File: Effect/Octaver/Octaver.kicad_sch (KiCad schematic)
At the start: 25 parts, among them J1 Conn_01x04_Pin, J2 Conn_01x04_Pin, Q1 MMBF5103, Q2 DMMT5551

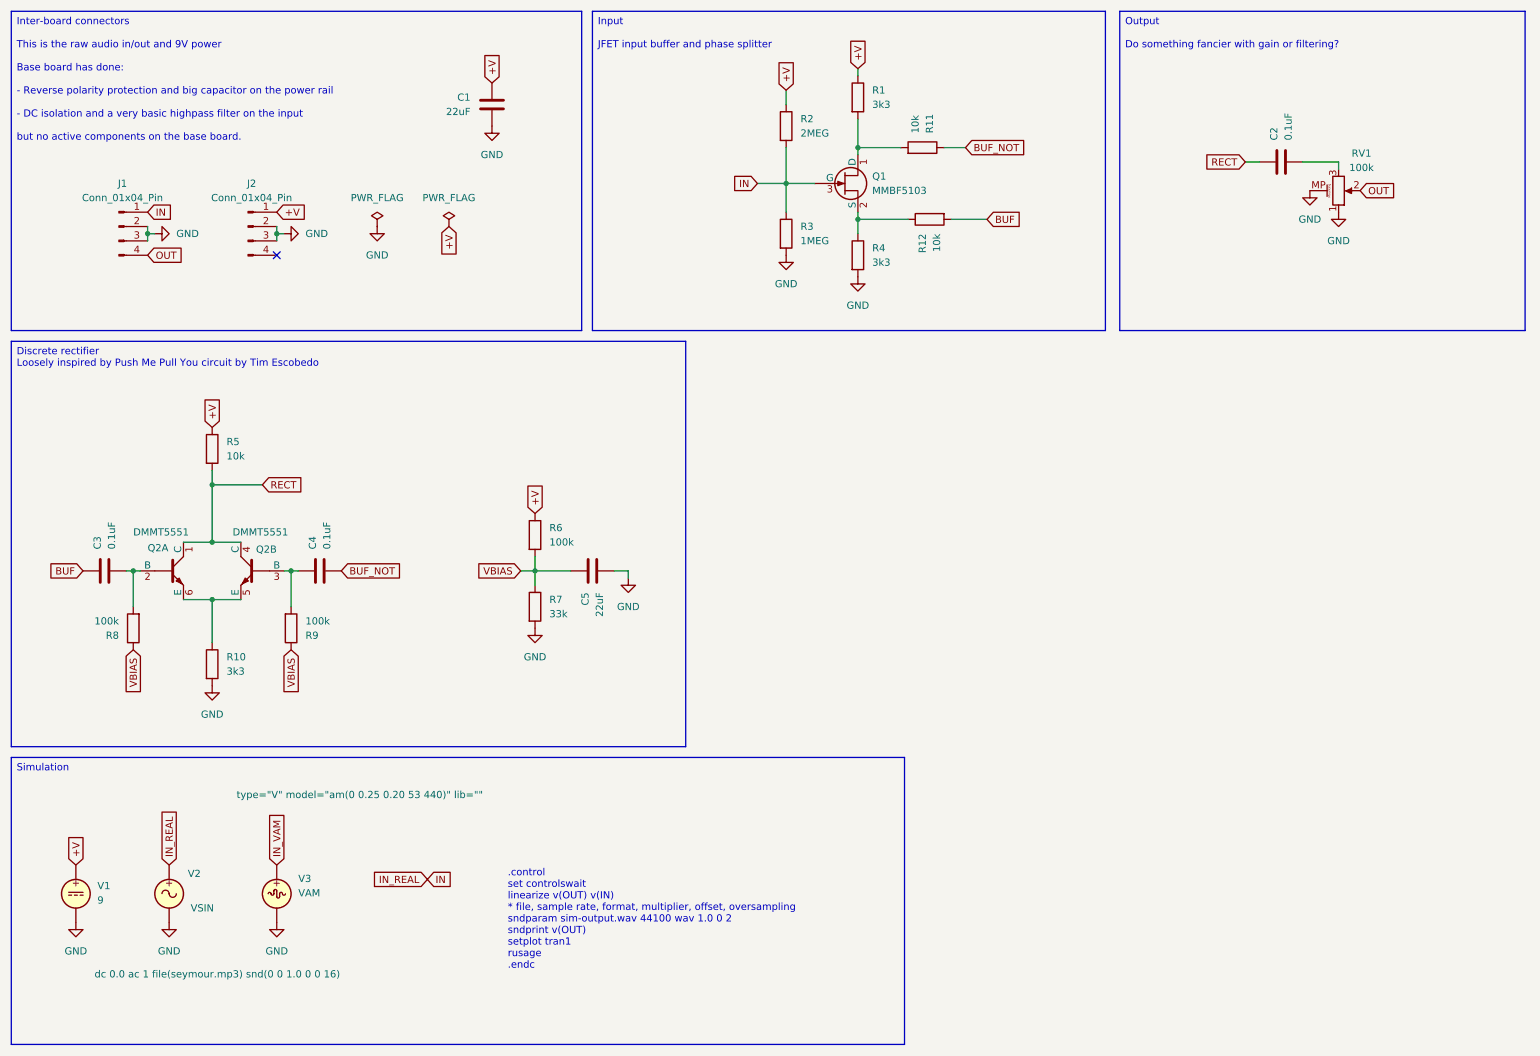
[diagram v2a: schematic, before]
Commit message: Update the Octaver circuit more, improve simulation
When I was trying to look up JFET phase splitter cicuits, I came up
suspiciously empty.  Adding the resistors between the phase splitter and
the rectification stage did fix things in simulation, but it all makes
me think somebody knows more than I do about this.

So since I wanted some amplification anyway, I put another BJT stage
there for the phase splitting, and one in the output stage for
amplification.

And I added the base board to the simulation, so that the whole input
signal rebiasing actually shows up for real.  With the DC-blocking
capacitor no longer on the effects board, the simulation ended up seeing
the signal input as a power source and that then made things all wonky.

Now, this is why I don't use op-amps any more: sane people do op-amp
circuits so that they don't have to worry about impedance issues.  But
insane people like me want to learn about these things, so...

That said, I think I really need to learn about feedback.  And not just
the "emitter degeneration resistor" kind.  Actual feedback between
stages (or even just from output back to transistor gate voltage for a
single transistor stage).

Signed-off-by: Linus Torvalds <torvalds@linux-foundation.org>
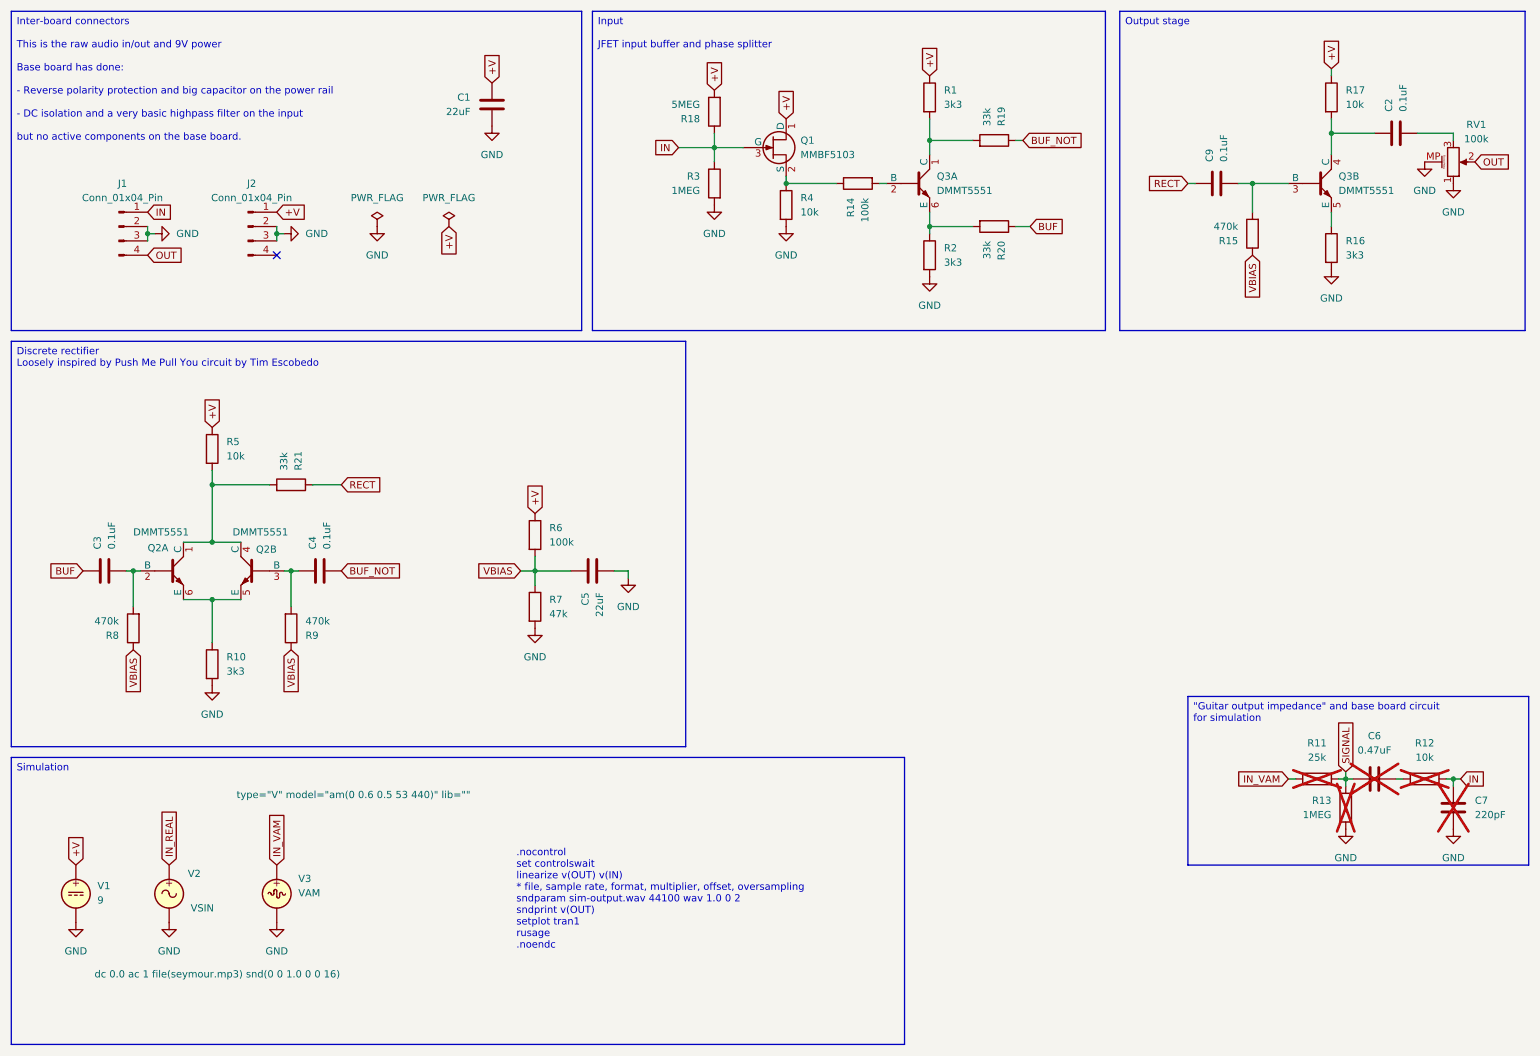
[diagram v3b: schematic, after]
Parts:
- added C6: 0.47uF, Capacitor_SMD:C_1206_3216Metric, symbol Device:C
- added C7: 220pF, Capacitor_SMD:C_0805_2012Metric_Pad1.18x1.45mm_HandSolder, symbol Device:C
- added C9: 0.1uF, Mylib:C_0704_1810Metric, symbol Device:C
- added Q3: DMMT5551, Package_TO_SOT_SMD:SOT-23-6, symbol Mylib:DMMT5551
- added R13: 1MEG, Resistor_SMD:R_0805_2012Metric, symbol Device:R
- added R14: 100k, Resistor_SMD:R_0805_2012Metric, symbol Device:R
- added R15: 470k, Resistor_SMD:R_0805_2012Metric, symbol Device:R
- added R16: 3k3, Resistor_SMD:R_0805_2012Metric, symbol Device:R
- added R17: 10k, Resistor_SMD:R_0805_2012Metric, symbol Device:R
- added R18: 5MEG, Resistor_SMD:R_0805_2012Metric, symbol Device:R
- added R19, R20, R21: 33k, Resistor_SMD:R_0805_2012Metric, symbol Device:R
- R11: value 10k -> 25k; footprint Resistor_SMD:R_0805_2012Metric -> Resistor_SMD:R_0805_2012Metric_Pad1.20x1.40mm_HandSolder; now not fitted; now left out of the parts list
- R12: footprint Resistor_SMD:R_0805_2012Metric -> Resistor_SMD:R_0805_2012Metric_Pad1.20x1.40mm_HandSolder; now not fitted; now left out of the parts list
- R2: value 2MEG -> 3k3
- R4: value 3k3 -> 10k
- R7: value 33k -> 47k
- R8, R9: value 100k -> 470k
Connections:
- net +V: now also Q1.1 (D), R17.1, R18.2; no longer R2.1
- net BUF: now also R20.1; no longer R12.2
- net BUF_NOT: now also R19.1; no longer R11.1
- net GND: now also R2.2, C7.2, R13.2, R16.2
- net IN: now also R12.2, C7.1, R18.1; no longer R2.2, V2.1
- net IN_VAM: now also R11.1
- net RECT: now also C9.1, R21.1; no longer C2.1, Q2.1 (C), Q2.4 (C), R5.2
- net VBIAS: now also R15.1
- net at Q1.2 (S), R4.1: now also R14.1; no longer R12.1
- new net: Q3.5 (E), R16.1
- new net: Q3.1 (C), R1.2, R19.2
- new net: Q3.6 (E), R2.1, R20.2
- new net: Q2.1 (C), Q2.4 (C), R21.2, R5.2
- new net: C6.2, R12.1
- new net: C9.2, Q3.3 (B), R15.2
- new net: C2.1, Q3.4 (C), R17.2
- new net: Q3.2 (B), R14.2
- new net IN_REAL: V2.1
- new net SIGNAL: C6.1, R11.2, R13.1
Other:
- note added: ".nocontrol set controlswait linearize v(OUT) v(IN) * file, sample rate, format, multiplier, offset, oversampling sndparam sim-output.wav 44100 wav 1.0 0 2 sndprint v(OUT) setplot tran1 rusage .noendc"
- note removed: ".control set controlswait linearize v(OUT) v(IN) * file, sample rate, format, multiplier, offset, oversampling sndparam sim-output.wav 44100 wav 1.0 0 2 sndprint v(OUT) setplot tran1 rusage .endc"
- moved on the sheet: C2, R3, R4, RV1

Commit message: More octaver circuit impedance tweaking
I decided that the JFET phase splitter is the right way to go after all,
and that I just need to make sure the output impedance is low enough for
the following circuit.  Smaller transistors, more current, stiffer
signals.

But "more current" in this case is still in the "a couple of mA" range,
and this isn't battery-operated, so to quote Alfred E Neuman: "What, me
worry?"

I'm not particularly happy with that output side, and I'll probably
continue to play with this to get a better feel for the whole input and
output impedance of the different transistor circuits.  But maybe it's
time to make another test pcb just to see if this works in reality at
all.

Signed-off-by: Linus Torvalds <torvalds@linux-foundation.org>
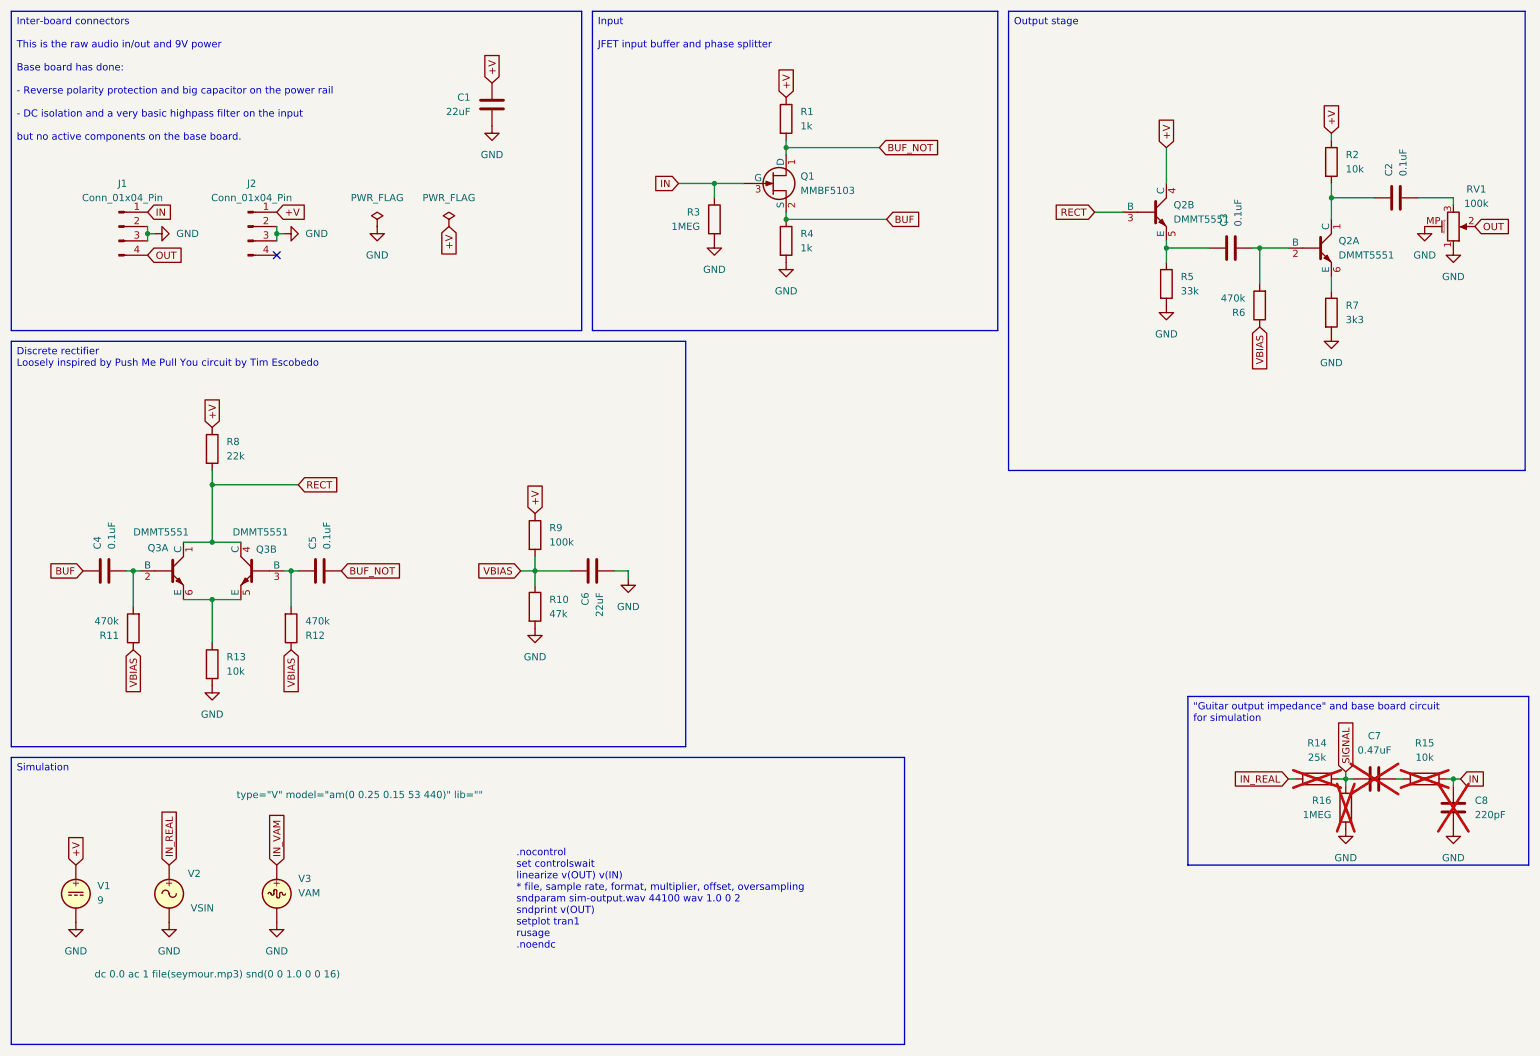
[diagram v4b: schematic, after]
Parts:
- removed C9: 0.1uF, Mylib:C_0704_1810Metric, symbol Device:C
- removed R14: 100k, Resistor_SMD:R_0805_2012Metric, symbol Device:R
- removed R15: 470k, Resistor_SMD:R_0805_2012Metric, symbol Device:R
- removed R18: 5MEG, Resistor_SMD:R_0805_2012Metric, symbol Device:R
- removed R19, R20, R21: 33k, Resistor_SMD:R_0805_2012Metric, symbol Device:R
- added C3: 0.1uF, Mylib:C_0704_1810Metric, symbol Device:C
- added R6: 470k, Resistor_SMD:R_0805_2012Metric, symbol Device:R
- R1: value 3k3 -> 1k
- R13: renamed from R10; value 3k3 -> 10k
- R4: value 10k -> 1k
- R5: renamed from R2; value 3k3 -> 33k
- R8: renamed from R5; value 10k -> 22k
- renumbered C3 to C4, C4 to C5, C5 to C6, C6 to C7, C7 to C8, Q3 to Q2, Q2 to Q3, R7 to R10, R8 to R11, R9 to R12, R11 to R14, R12 to R15, R13 to R16, R17 to R2, R16 to R7, R6 to R9
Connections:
- net +V: now also Q2.4 (C); no longer Q1.1 (D)
- net BUF: now also Q1.2 (S), R4.1
- net BUF_NOT: now also Q1.1 (D), R1.2
- net IN_REAL: now also R14.1
- net IN_VAM: no longer R14.1
- net RECT: now also Q2.3 (B), Q3.1 (C), Q3.4 (C), R8.2
- net VBIAS: now also R6.1
- net at R7.1: now also Q2.6 (E); no longer Q2.5 (E)
- net at Q2.1 (C): now also C2.1, R2.2; no longer R1.2
- net at R5.1: now also Q2.5 (E), C3.1; no longer Q2.6 (E)
- net at Q2.2 (B): now also C3.2, R6.2
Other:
- moved on the sheet: C2, Q1, Q2A, Q2B, R2, R3, R4, R5, R7, RV1

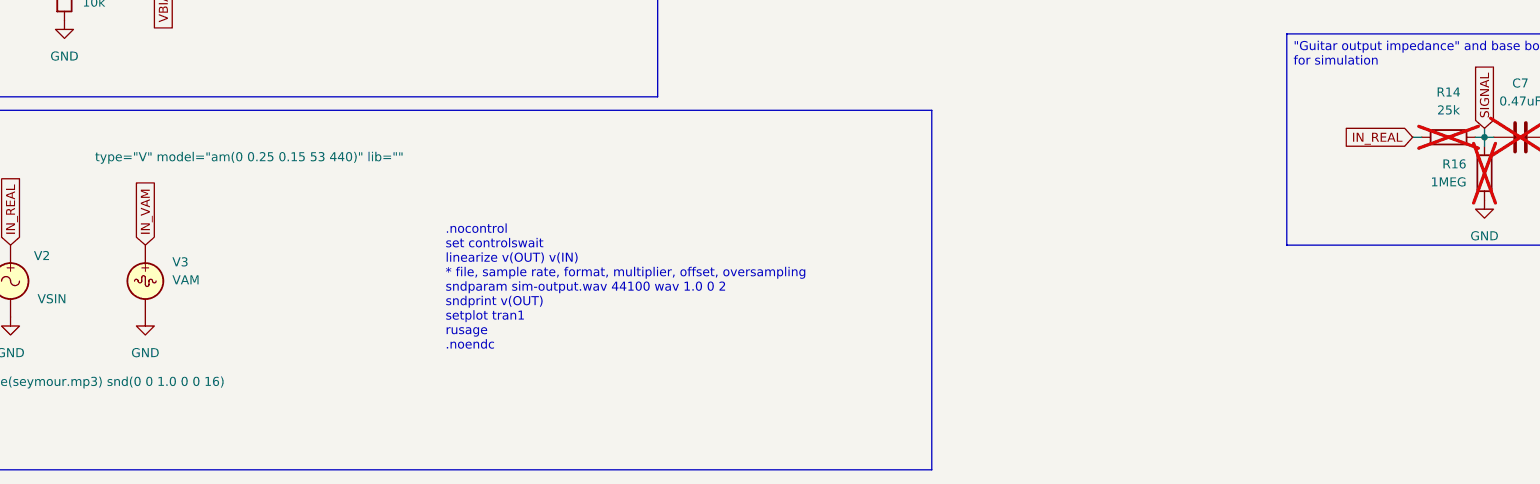
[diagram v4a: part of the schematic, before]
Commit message: Add 20Hz triangle wave to Octaver simulation
Good for checking bass response, and shows that I need to pick bigger
capacitors.

Signed-off-by: Linus Torvalds <torvalds@linux-foundation.org>
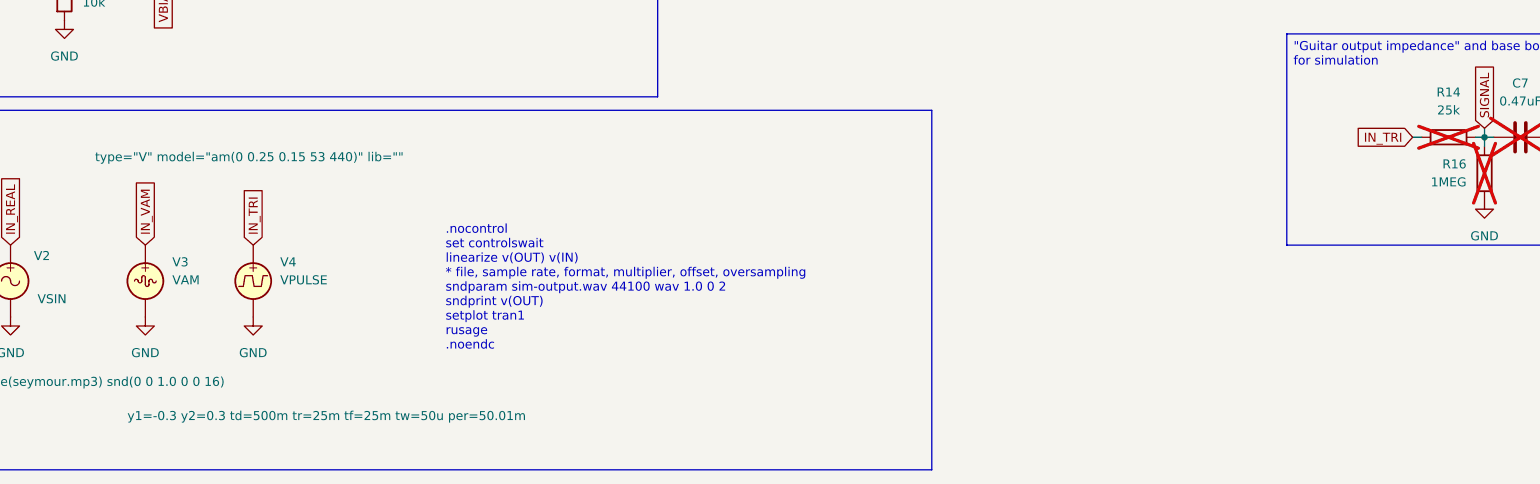
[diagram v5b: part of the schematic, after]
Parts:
- added V4: VPULSE, symbol Simulation_SPICE:VPULSE
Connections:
- net GND: now also V4.2
- net IN_REAL: no longer R14.1
- new net IN_TRI: R14.1, V4.1
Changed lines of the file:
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@@
 		)
 	)
-	(global_label "IN_REAL"
+	(global_label "IN_TRI"
 		(shape input)
 		(at 240.03 149.86 180)
@@
 		)
 		(property "Intersheetrefs" "${INTERSHEET_REFS}"
-			(at 229.6062 149.86 0)
+			(at 231.2995 149.86 0)
 			(hide yes)
 			(effects
@@
 		)
 	)
+	(global_label "IN_TRI"
+		(shape input)
+		(at 76.2 165.1 90)
+		(fields_autoplaced yes)
+		(effects
+			(font
+				(size 1.27 1.27)
+			)
+			(justify left)
+		)
+		(property "Intersheetrefs" "${INTERSHEET_REFS}"
+			(at 76.2 156.3695 90)
+			(hide yes)
+			(effects
+				(font
+					(size 1.27 1.27)
+				)
+				(justify left)
+			)
+		)
+	)
 	(global_label "IN"
 		(shape input)
@@
 	)
 	(symbol
+		(lib_id "Simulation_SPICE:VPULSE")
+		(at 76.2 170.18 0)
+		(unit 1)
+		(exclude_from_sim no)
+		(in_bom no)
+		(on_board no)
+		(dnp no)
+		(property "Reference" "V4"
+			(at 80.01 167.5101 0)
+			(effects
+				(font
+					(size 1.27 1.27)
+				)
+				(justify left)
+			)
+		)
+		(property "Value" "VPULSE"
+			(at 80.01 170.0501 0)
+			(effects
+				(font
+					(size 1.27 1.27)
+				)
+				(justify left)
+			)
+		)
+		(property "Footprint" ""
+			(at 76.2 170.18 0)
+			(hide yes)
+			(effects
+				(font
+					(size 1.27 1.27)
+				)
+			)
+		)
+		(property "Datasheet" "https://ngspice.sourceforge.io/docs/ngspice-html-manual/manual.xhtml#sec_Independent_Sources_for"
+			(at 76.2 170.18 0)
+			(hide yes)
+			(effects
+				(font
+					(size 1.27 1.27)
+				)
+			)
+		)
+		(property "Description" "Voltage source, pulse"
+			(at 76.2 170.18 0)
+			(hide yes)
+			(effects
+				(font
+					(size 1.27 1.27)
+				)
+			)
+		)
+		(property "Sim.Pins" "1=+ 2=-"
+			(at 76.2 170.18 0)
+			(hide yes)
+			(effects
+				(font
+					(size 1.27 1.27)
+				)
+			)
+		)
+		(property "Sim.Type" "PULSE"
+			(at 76.2 170.18 0)
+			(hide yes)
+			(effects
+				(font
+					(size 1.27 1.27)
+				)
+			)
+		)
+		(property "Sim.Device" "V"
+			(at 76.2 170.18 0)
+			(hide yes)
+			(effects
+				(font
+					(size 1.27 1.27)
+				)
+				(justify left)
+			)
+		)
+		(property "Sim.Params" "y1=-0.3 y2=0.3 td=500m tr=25m tf=25m tw=50u per=50.01m"
+			(at 58.42 189.23 0)
+			(effects
+				(font
+					(size 1.27 1.27)
+				)
+				(justify left)
+			)
+		)
+		(pin "1"
+		)
+		(pin "2"
+		)
+		(instances
+			(project "Octaver"
+				(path "/9e337e0b-885b-4d2b-99a2-62cdd082c615"
+					(reference "V4")
+					(unit 1)
+				)
+			)
+		)
+	)
+	(symbol
 		(lib_id "power:GND")
 		(at 39.37 53.34 90)
@@
 					(unit 1)
 				)
+			)
+		)
+	)
+	(symbol
+		(lib_id "power:GND")
+		(at 76.2 175.26 0)
+		(unit 1)
+		(exclude_from_sim no)
+		(in_bom yes)
+		(on_board yes)
+		(dnp no)
+		(fields_autoplaced yes)
+		(property "Reference" "#PWR024"
+			(at 76.2 181.61 0)
+			(hide yes)
+			(effects
+				(font
+					(size 1.27 1.27)
+				)
+			)
+		)
+		(property "Value" "GND"
+			(at 76.2 180.34 0)
+			(effects
+				(font
+					(size 1.27 1.27)
+				)
+			)
+		)
+		(property "Footprint" ""
+			(at 76.2 175.26 0)
+			(hide yes)
+			(effects
+				(font
+					(size 1.27 1.27)
+				)
+			)
+		)
+		(property "Datasheet" ""
+			(at 76.2 175.26 0)
+			(hide yes)
+			(effects
+				(font
+					(size 1.27 1.27)
+				)
+			)
+		)
+		(property "Description" "Power symbol creates a global label with name \"GND\" , ground"
+			(at 76.2 175.26 0)
+			(hide yes)
+			(effects
+				(font
+					(size 1.27 1.27)
+				)
+			)
+		)
+		(pin "1"
+		)
+		(instances
+			(project "Octaver"
+				(path "/9e337e0b-885b-4d2b-99a2-62cdd082c615"
+					(reference "#PWR024")
+					(unit 1)
+				)
